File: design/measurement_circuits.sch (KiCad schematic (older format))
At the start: 0 parts

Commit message: Fixing connection errors
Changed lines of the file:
@@
 F0 "voltage" 60
 F1 "voltage.sch" 60
-F2 "Phase_In" I L 1765 1078 60
-F3 "Voltage_AD" O R 2790 1673 60
-F4 "Neutral_Filtered" I L 1765 1328 60
+F2 "Voltage_AD" O R 2790 1673 60
+F3 "Neutral_Filtered" I L 1765 1328 60
+F4 "Phase_Line" I L 1765 1078 60
 $EndSheet
 $Sheet
@@
 $EndSheet
 Text HLabel 1690 1078 0    60   Input ~ 0
-Phase_ln
+Phase_Line
 Text HLabel 1640 2455 0    60   Input ~ 0
 CT1_1

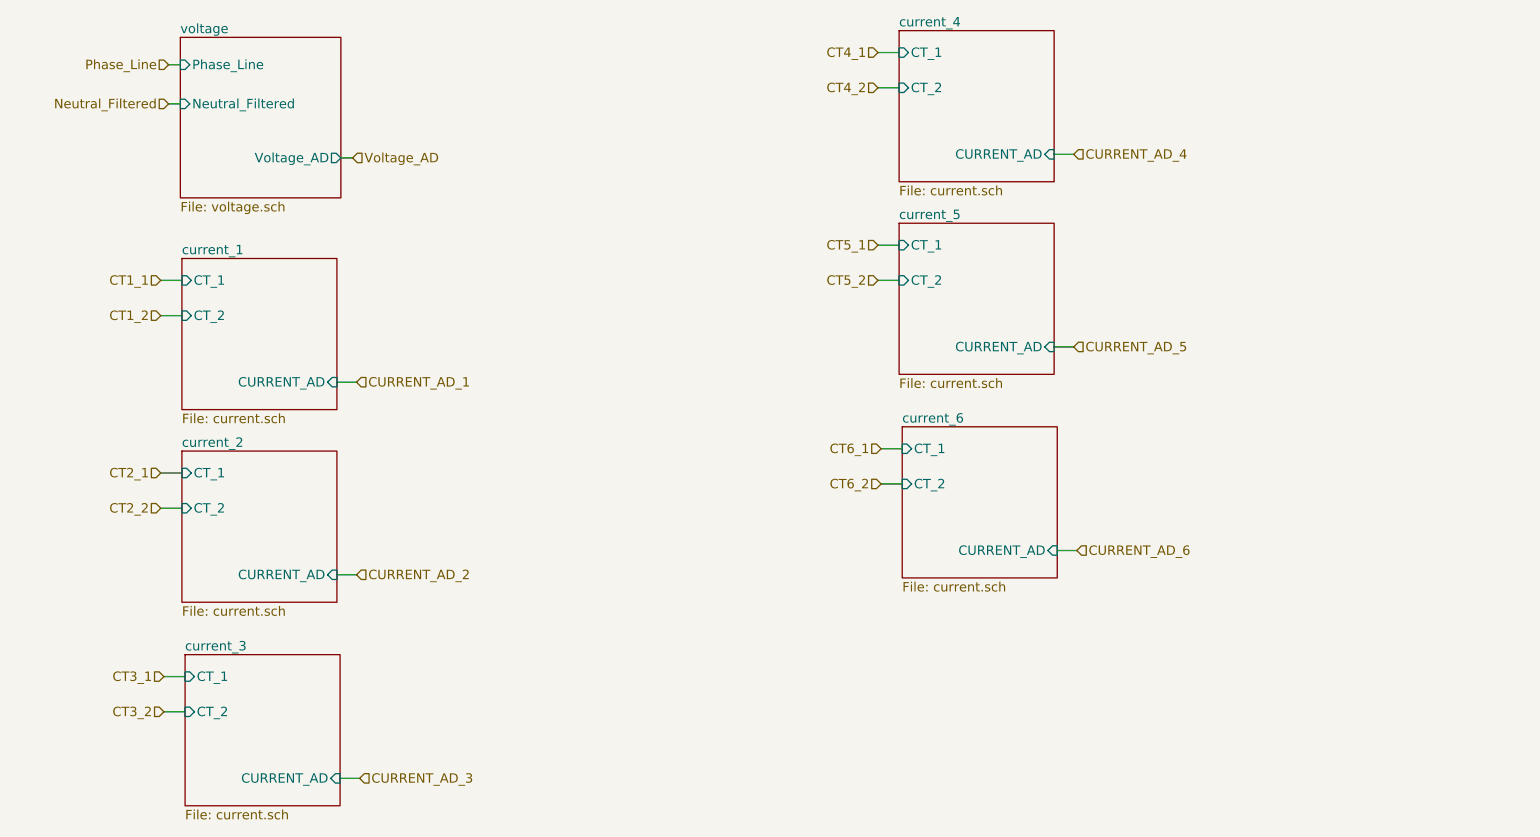
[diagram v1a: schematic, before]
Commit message: Agrego los dos circuitos extra para medir tension
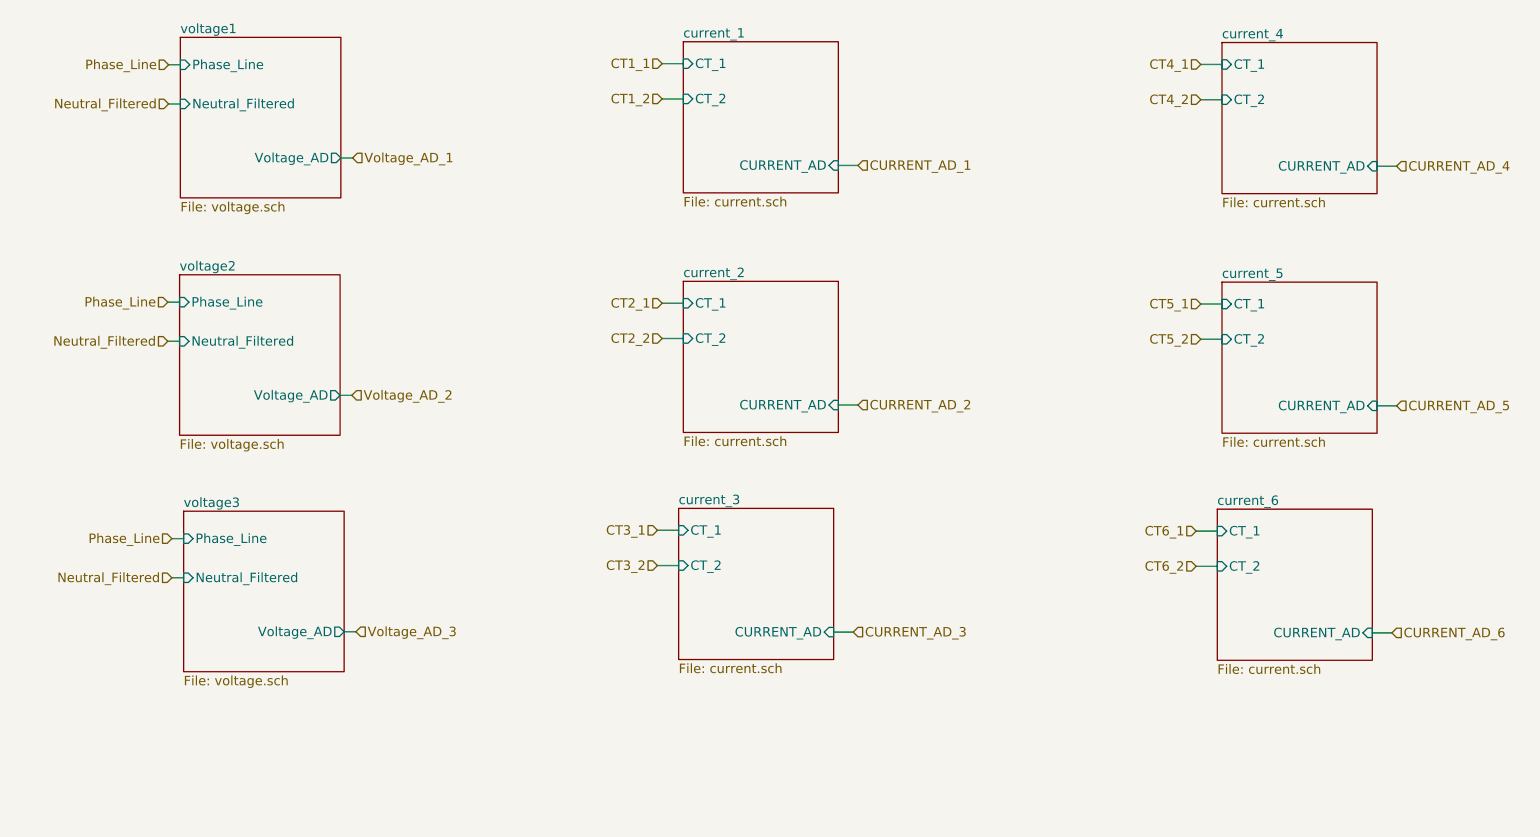
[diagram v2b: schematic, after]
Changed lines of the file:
@@
 LIBS:memory
 LIBS:xilinx
-LIBS:special
 LIBS:microcontrollers
 LIBS:dsp
@@
 $Descr A4 11693 8268
 encoding utf-8
-Sheet 11 18
+Sheet 11 20
 Title "PIVI"
 Date "Mon 27 Jul 2015"
@@
 S 1765 903  1025 1025
 U 55B216B6
-F0 "voltage" 60
+F0 "voltage1" 60
 F1 "voltage.sch" 60
 F2 "Voltage_AD" O R 2790 1673 60
@@
 $EndSheet
 $Sheet
-S 1775 2315 990  965
+S 4977 931  990  965
 U 55B266EE
 F0 "current_1" 60
 F1 "current.sch" 60
-F2 "CT_1" I L 1775 2455 60
-F3 "CT_2" I L 1775 2680 60
-F4 "CURRENT_AD" I R 2765 3105 60
+F2 "CT_1" I L 4977 1071 60
+F3 "CT_2" I L 4977 1296 60
+F4 "CURRENT_AD" I R 5967 1721 60
 $EndSheet
 Text HLabel 1690 1078 0    60   Input ~ 0
 Phase_Line
-Text HLabel 1640 2455 0    60   Input ~ 0
+Text HLabel 4842 1071 0    60   Input ~ 0
 CT1_1
-Text HLabel 1640 2680 0    60   Input ~ 0
+Text HLabel 4842 1296 0    60   Input ~ 0
 CT1_2
-Text HLabel 2890 3105 2    60   Input ~ 0
+Text HLabel 6092 1721 2    60   Input ~ 0
 CURRENT_AD_1
 $Sheet
-S 1775 3545 990  965
+S 4977 2461 990  965
 U 55B3A3F6
 F0 "current_2" 60
 F1 "current.sch" 60
-F2 "CT_1" I L 1775 3685 60
-F3 "CT_2" I L 1775 3910 60
-F4 "CURRENT_AD" I R 2765 4335 60
-$EndSheet
-Text HLabel 1640 3685 0    60   Input ~ 0
+F2 "CT_1" I L 4977 2601 60
+F3 "CT_2" I L 4977 2826 60
+F4 "CURRENT_AD" I R 5967 3251 60
+$EndSheet
+Text HLabel 4842 2601 0    60   Input ~ 0
 CT2_1
-Text HLabel 1640 3910 0    60   Input ~ 0
+Text HLabel 4842 2826 0    60   Input ~ 0
 CT2_2
-Text HLabel 2890 4335 2    60   Input ~ 0
+Text HLabel 6092 3251 2    60   Input ~ 0
 CURRENT_AD_2
 $Sheet
-S 1795 4845 990  965
+S 4947 3911 990  965
 U 55B3A74F
 F0 "current_3" 60
 F1 "current.sch" 60
-F2 "CT_1" I L 1795 4985 60
-F3 "CT_2" I L 1795 5210 60
-F4 "CURRENT_AD" I R 2785 5635 60
-$EndSheet
-Text HLabel 1660 4985 0    60   Input ~ 0
+F2 "CT_1" I L 4947 4051 60
+F3 "CT_2" I L 4947 4276 60
+F4 "CURRENT_AD" I R 5937 4701 60
+$EndSheet
+Text HLabel 4812 4051 0    60   Input ~ 0
 CT3_1
-Text HLabel 1660 5210 0    60   Input ~ 0
+Text HLabel 4812 4276 0    60   Input ~ 0
 CT3_2
-Text HLabel 2910 5635 2    60   Input ~ 0
+Text HLabel 6062 4701 2    60   Input ~ 0
 CURRENT_AD_3
 $Sheet
-S 6355 860  990  965
+S 8417 936  990  965
 U 55B3BD6E
 F0 "current_4" 60
 F1 "current.sch" 60
-F2 "CT_1" I L 6355 1000 60
-F3 "CT_2" I L 6355 1225 60
-F4 "CURRENT_AD" I R 7345 1650 60
-$EndSheet
-Text HLabel 6220 1000 0    60   Input ~ 0
+F2 "CT_1" I L 8417 1076 60
+F3 "CT_2" I L 8417 1301 60
+F4 "CURRENT_AD" I R 9407 1726 60
+$EndSheet
+Text HLabel 8282 1076 0    60   Input ~ 0
 CT4_1
-Text HLabel 6220 1225 0    60   Input ~ 0
+Text HLabel 8282 1301 0    60   Input ~ 0
 CT4_2
-Text HLabel 7470 1650 2    60   Input ~ 0
+Text HLabel 9532 1726 2    60   Input ~ 0
 CURRENT_AD_4
 $Sheet
-S 6355 2090 990  965
+S 8417 2466 990  965
 U 55B3BD79
 F0 "current_5" 60
 F1 "current.sch" 60
-F2 "CT_1" I L 6355 2230 60
-F3 "CT_2" I L 6355 2455 60
-F4 "CURRENT_AD" I R 7345 2880 60
-$EndSheet
-Text HLabel 6220 2230 0    60   Input ~ 0
+F2 "CT_1" I L 8417 2606 60
+F3 "CT_2" I L 8417 2831 60
+F4 "CURRENT_AD" I R 9407 3256 60
+$EndSheet
+Text HLabel 8282 2606 0    60   Input ~ 0
 CT5_1
-Text HLabel 6220 2455 0    60   Input ~ 0
+Text HLabel 8282 2831 0    60   Input ~ 0
 CT5_2
-Text HLabel 7470 2880 2    60   Input ~ 0
+Text HLabel 9532 3256 2    60   Input ~ 0
 CURRENT_AD_5
 $Sheet
-S 6375 3390 990  965
+S 8387 3916 990  965
 U 55B3BD84
 F0 "current_6" 60
 F1 "current.sch" 60
-F2 "CT_1" I L 6375 3530 60
-F3 "CT_2" I L 6375 3755 60
-F4 "CURRENT_AD" I R 7365 4180 60
-$EndSheet
-Text HLabel 6240 3530 0    60   Input ~ 0
+F2 "CT_1" I L 8387 4056 60
+F3 "CT_2" I L 8387 4281 60
+F4 "CURRENT_AD" I R 9377 4706 60
+$EndSheet
+Text HLabel 8252 4056 0    60   Input ~ 0
 CT6_1
-Text HLabel 6240 3755 0    60   Input ~ 0
+Text HLabel 8252 4281 0    60   Input ~ 0
 CT6_2
-Text HLabel 7490 4180 2    60   Input ~ 0
+Text HLabel 9502 4706 2    60   Input ~ 0
 CURRENT_AD_6
 Text HLabel 2865 1673 2    60   Input ~ 0
-Voltage_AD
+Voltage_AD_1
 Wire Wire Line
 	1690 1078 1765 1078
@@
 	1690 1328 1765 1328
 Wire Wire Line
-	1775 2455 1640 2455
-Wire Wire Line
-	1640 2680 1775 2680
-Wire Wire Line
-	2765 3105 2890 3105
-Wire Wire Line
-	1775 3685 1640 3685
-Wire Wire Line
-	1640 3910 1775 3910
-Wire Wire Line
-	2765 4335 2890 4335
-Wire Wire Line
-	1795 4985 1660 4985
-Wire Wire Line
-	1660 5210 1795 5210
-Wire Wire Line
-	2785 5635 2910 5635
-Wire Wire Line
-	6355 1000 6220 1000
-Wire Wire Line
-	6220 1225 6355 1225
-Wire Wire Line
-	7345 1650 7470 1650
-Wire Wire Line
-	6355 2230 6220 2230
-Wire Wire Line
-	6220 2455 6355 2455
-Wire Wire Line
-	7345 2880 7470 2880
-Wire Wire Line
-	6375 3530 6240 3530
-Wire Wire Line
-	6240 3755 6375 3755
-Wire Wire Line
-	7365 4180 7490 4180
+	4977 1071 4842 1071
+Wire Wire Line
+	4842 1296 4977 1296
+Wire Wire Line
+	5967 1721 6092 1721
+Wire Wire Line
+	4977 2601 4842 2601
+Wire Wire Line
+	4842 2826 4977 2826
+Wire Wire Line
+	5967 3251 6092 3251
+Wire Wire Line
+	4947 4051 4812 4051
+Wire Wire Line
+	4812 4276 4947 4276
+Wire Wire Line
+	5937 4701 6062 4701
+Wire Wire Line
+	8417 1076 8282 1076
+Wire Wire Line
+	8282 1301 8417 1301
+Wire Wire Line
+	9407 1726 9532 1726
+Wire Wire Line
+	8417 2606 8282 2606
+Wire Wire Line
+	8282 2831 8417 2831
+Wire Wire Line
+	9407 3256 9532 3256
+Wire Wire Line
+	8387 4056 8252 4056
+Wire Wire Line
+	8252 4281 8387 4281
+Wire Wire Line
+	9377 4706 9502 4706
 Wire Wire Line
 	2790 1673 2865 1673
 Text HLabel 1690 1328 0    60   Input ~ 0
 Neutral_Filtered
+$Sheet
+S 1760 2419 1025 1025
+U 55B9EDA2
+F0 "voltage2" 60
+F1 "voltage.sch" 60
+F2 "Voltage_AD" O R 2785 3189 60
+F3 "Neutral_Filtered" I L 1760 2844 60
+F4 "Phase_Line" I L 1760 2594 60
+$EndSheet
+Text HLabel 1685 2594 0    60   Input ~ 0
+Phase_Line
+Text HLabel 2860 3189 2    60   Input ~ 0
+Voltage_AD_2
+Wire Wire Line
+	1685 2594 1760 2594
+Wire Wire Line
+	1685 2844 1760 2844
+Wire Wire Line
+	2785 3189 2860 3189
+Text HLabel 1685 2844 0    60   Input ~ 0
+Neutral_Filtered
+$Sheet
+S 1786 3929 1025 1025
+U 55BA09A0
+F0 "voltage3" 60
+F1 "voltage.sch" 60
+F2 "Voltage_AD" O R 2811 4699 60
+F3 "Neutral_Filtered" I L 1786 4354 60
+F4 "Phase_Line" I L 1786 4104 60
+$EndSheet
+Text HLabel 1711 4104 0    60   Input ~ 0
+Phase_Line
+Text HLabel 2886 4699 2    60   Input ~ 0
+Voltage_AD_3
+Wire Wire Line
+	1711 4104 1786 4104
+Wire Wire Line
+	1711 4354 1786 4354
+Wire Wire Line
+	2811 4699 2886 4699
+Text HLabel 1711 4354 0    60   Input ~ 0
+Neutral_Filtered
 $EndSCHEMATC
